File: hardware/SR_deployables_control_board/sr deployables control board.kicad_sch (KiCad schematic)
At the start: 26 parts, among them J1 Conn_01x12_Pin, J2 Conn_01x02_Pin, J3 Conn_01x07_Pin, Q3 2N7002, Q4 2N7002, U1 MCP3002, U2 DRV8833PW

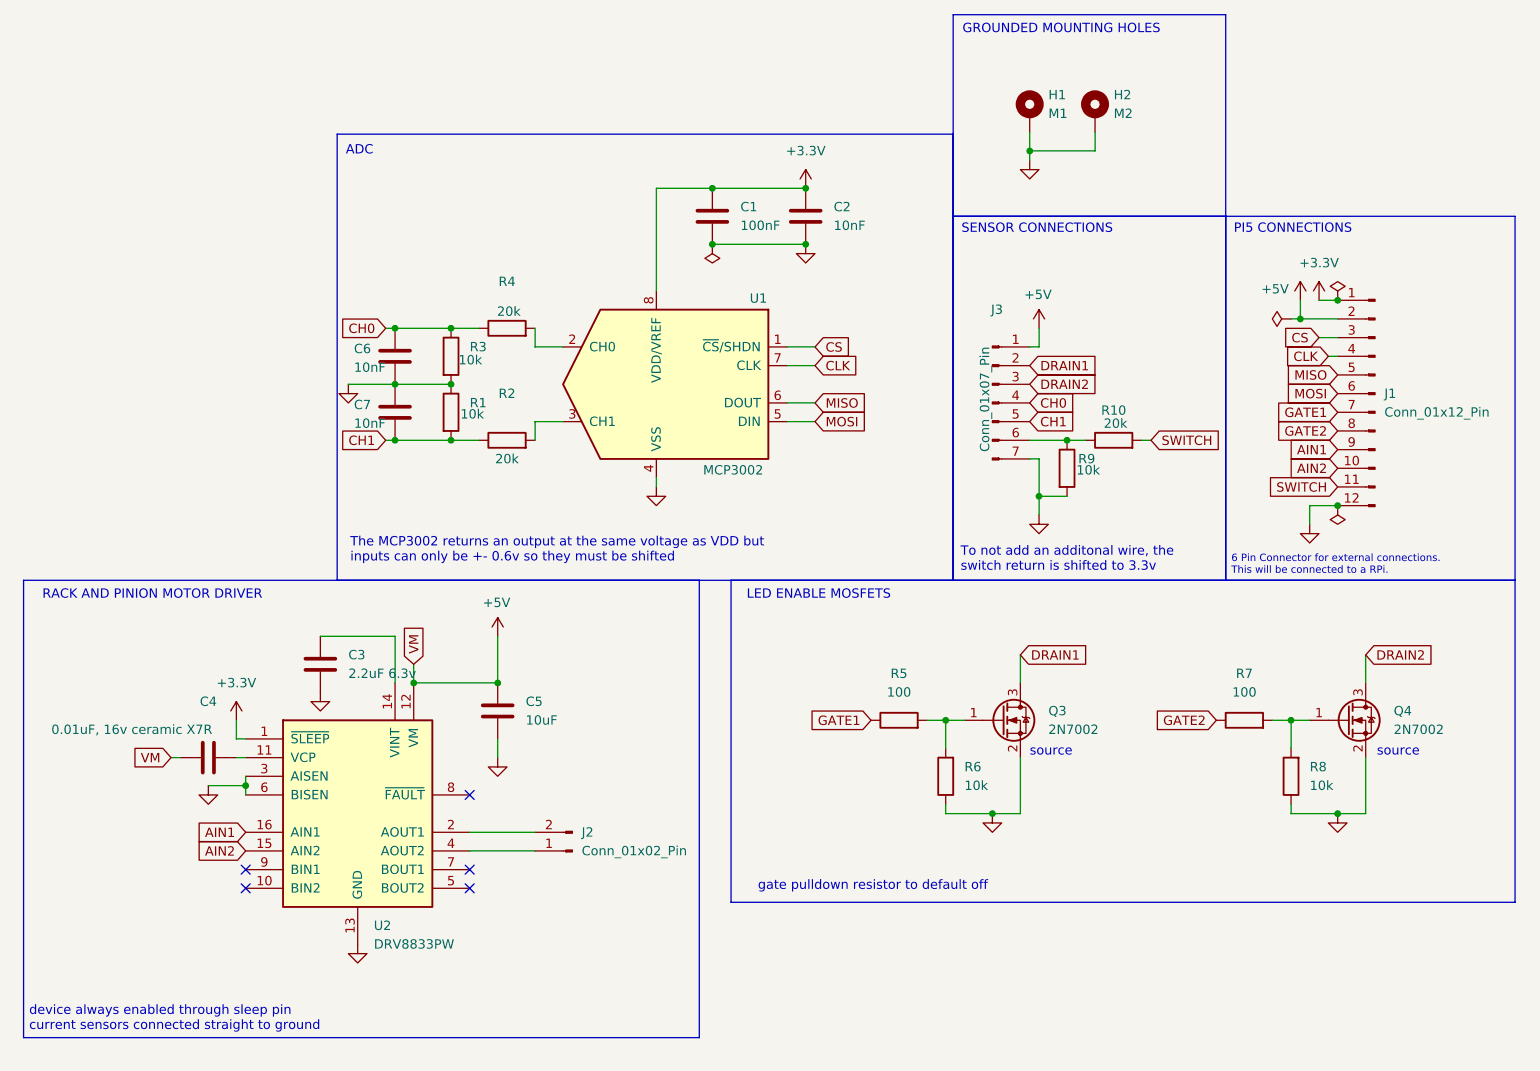
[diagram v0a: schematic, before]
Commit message: feat: New motor driver/pi interface pcb for kibisis & space resources
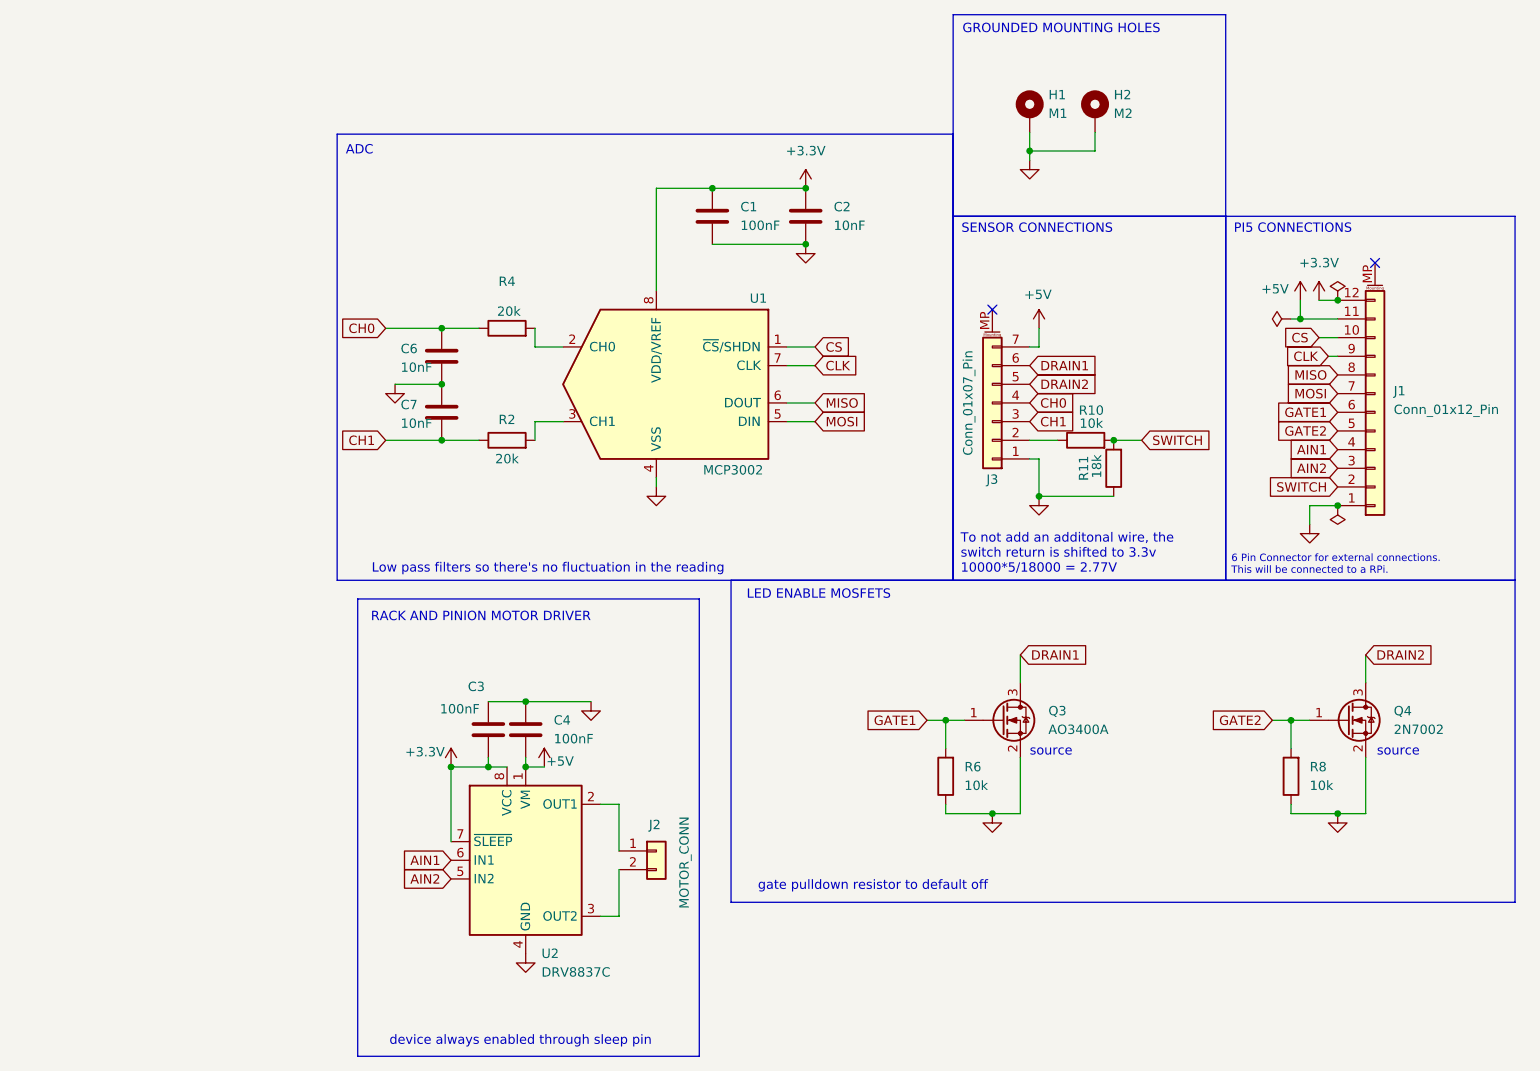
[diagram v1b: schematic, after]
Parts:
- removed C5: 10uF, Capacitor_SMD:C_0805_2012Metric_Pad1.18x1.45mm_HandSolder, symbol Device:C
- removed J2: Conn_01x02_Pin, Connector_PinHeader_2.54mm:PinHeader_1x02_P2.54mm_Vertical, symbol Connector:Conn_01x02_Pin
- removed R1, R3, R9: 10k, Resistor_SMD:R_0805_2012Metric_Pad1.20x1.40mm_HandSolder, symbol Device:R
- removed R5, R7: 100, Resistor_SMD:R_0805_2012Metric_Pad1.20x1.40mm_HandSolder, symbol Device:R
- removed U2: DRV8833PW, Package_SO:TSSOP-16-1EP_4.4x5mm_P0.65mm_EP3x3mm_ThermalVias, symbol Driver_Motor:DRV8833PW
- added J2: MOTOR_CONN, Connector_JST:JST_XH_B2B-XH-A_1x02_P2.50mm_Vertical, symbol Connector_Generic:Conn_01x02
- added R11: 18k, Resistor_SMD:R_0805_2012Metric_Pad1.20x1.40mm_HandSolder, symbol Device:R
- added U2: DRV8837C, Package_SON:WSON-8-1EP_2x2mm_P0.5mm_EP0.9x1.6mm, symbol Driver_Motor:DRV8837C
- C3: value 2.2uF 6.3v -> 100nF
- C4: value 0.01uF, 16v ceramic X7R -> 100nF
- H1, H2: footprint MountingHole:MountingHole_2.2mm_M2_Pad_Via -> MountingHole:MountingHole_3.2mm_M3_Pad_Via
- J1: footprint Connector_JST:JST_GH_BM12B-GHS-TBT_1x12-1MP_P1.25mm_Vertical -> Connector_JST:JST_ZH_S12B-ZR-SM4A-TF_1x12-1MP_P1.50mm_Horizontal; symbol Connector:Conn_01x12_Pin -> Connector_Generic_MountingPin:Conn_01x12_MountingPin
- J3: footprint Connector_JST:JST_GH_BM07B-GHS-TBT_1x07-1MP_P1.25mm_Vertical -> Connector_JST:JST_ZH_S7B-ZR-SM4A-TF_1x07-1MP_P1.50mm_Horizontal; symbol Connector:Conn_01x07_Pin -> Connector_Generic_MountingPin:Conn_01x07_MountingPin
- Q3: value 2N7002 -> AO3400A
- R10: value 20k -> 10k
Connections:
- net +3.3V: now also C3.2, J1.12 (Pin_12), U2.7 (~{SLEEP}), U2.8 (VCC); no longer J1.1 (Pin_1)
- net +5V: now also C4.2, J1.11 (Pin_11), J3.7 (Pin_7), U2.1 (VM); no longer C4.1, J1.2 (Pin_2), J3.1 (Pin_1)
- net AIN1: now also J1.4 (Pin_4), U2.6 (IN1); no longer J1.9 (Pin_9)
- net AIN2: now also J1.3 (Pin_3), U2.5 (IN2); no longer J1.10 (Pin_10)
- net CH1: now also J3.3 (Pin_3); no longer J3.5 (Pin_5)
- net CLK: now also J1.9 (Pin_9); no longer J1.4 (Pin_4)
- net CS: now also J1.10 (Pin_10); no longer J1.3 (Pin_3)
- net DRAIN1: now also J3.6 (Pin_6); no longer J3.2 (Pin_2)
- net DRAIN2: now also J3.5 (Pin_5); no longer J3.3 (Pin_3)
- net GATE1: now also J1.6 (Pin_6), Q3.1 (G), R6.2; no longer J1.7 (Pin_7)
- net GATE2: now also J1.5 (Pin_5), Q4.1 (G), R8.2; no longer J1.8 (Pin_8)
- net GND: now also C3.1, C4.1, J1.1 (Pin_1), J3.1 (Pin_1), R11.1, U2.4 (GND), U2.9 (GND); no longer C3.2, J1.12 (Pin_12), J3.7 (Pin_7)
- net MISO: now also J1.8 (Pin_8); no longer J1.5 (Pin_5)
- net MOSI: now also J1.7 (Pin_7); no longer J1.6 (Pin_6)
- net SWITCH: now also J1.2 (Pin_2), R11.2; no longer J1.11 (Pin_11)
- net at R10.1: now also J3.2 (Pin_2); no longer J3.6 (Pin_6)
- new net: J2.1 (Pin_1), U2.2 (OUT1)
- new net: J2.2 (Pin_2), U2.3 (OUT2)
- no-connect marks 5 -> 2
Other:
- note added: "Low pass filters so there's no fluctuation in the reading"
- note added: "To not add an additonal wire, the switch return is shifted to 3.3v 10000*5/18000 = 2.77V"
- note added: "device always enabled through sleep pin"
- note removed: "The MCP3002 returns an output at the same voltage as VDD but inputs can only be +- 0.6v so they must be shifted"
- note removed: "To not add an additonal wire, the switch return is shifted to 3.3v"
- note removed: "device always enabled through sleep pin current sensors connected straight to ground"
- moved on the sheet: C6, C7, R10

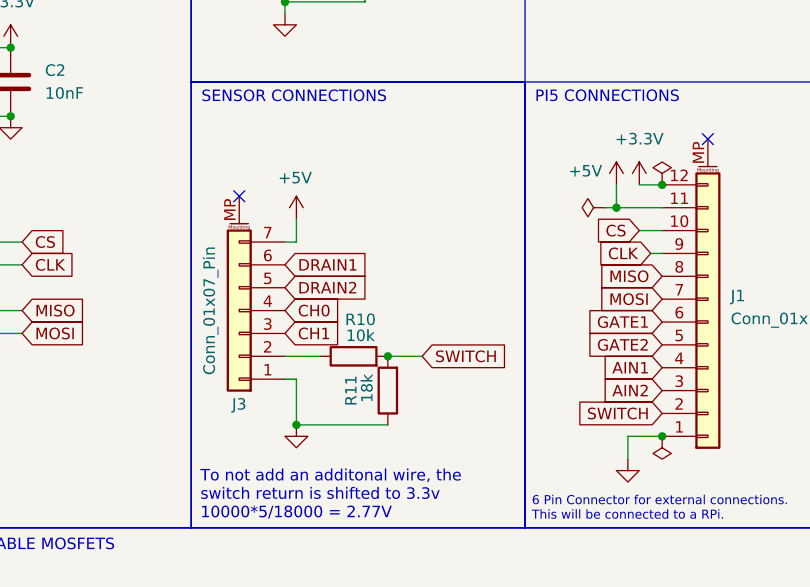
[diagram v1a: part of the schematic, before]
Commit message: Retraced voltage divider
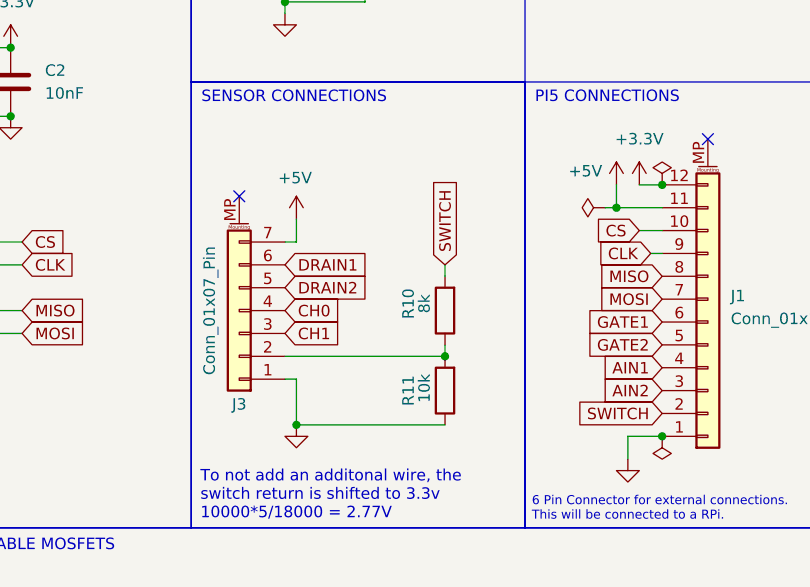
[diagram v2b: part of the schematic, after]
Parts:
- R10: value 10k -> 8k
- R11: value 18k -> 10k
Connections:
- net SWITCH: no longer R11.2
- net at J3.2 (Pin_2), R10.1: now also R11.2
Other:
- moved on the sheet: R10, R11
